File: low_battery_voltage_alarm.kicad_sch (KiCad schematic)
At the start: 20 parts, among them J1 V-DISPLAY, Q1 2N4401, Q2 2N4401, SW1 SW_DIP_x01, U1 NE555P

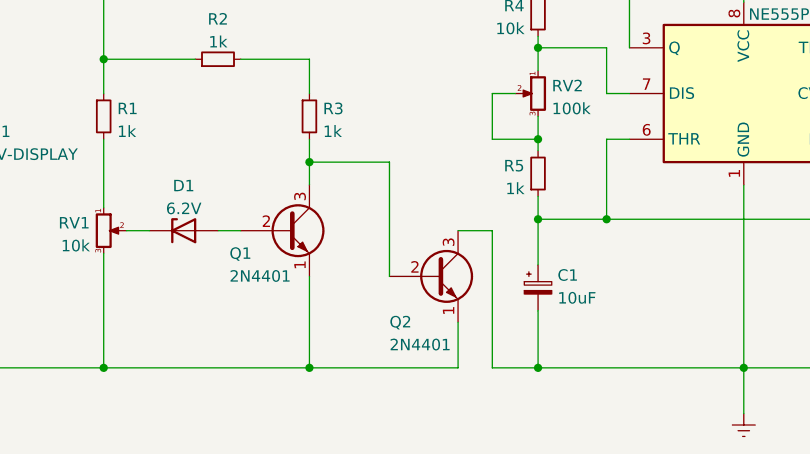
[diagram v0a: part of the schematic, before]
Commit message: change 2N4401 => MMBT4401
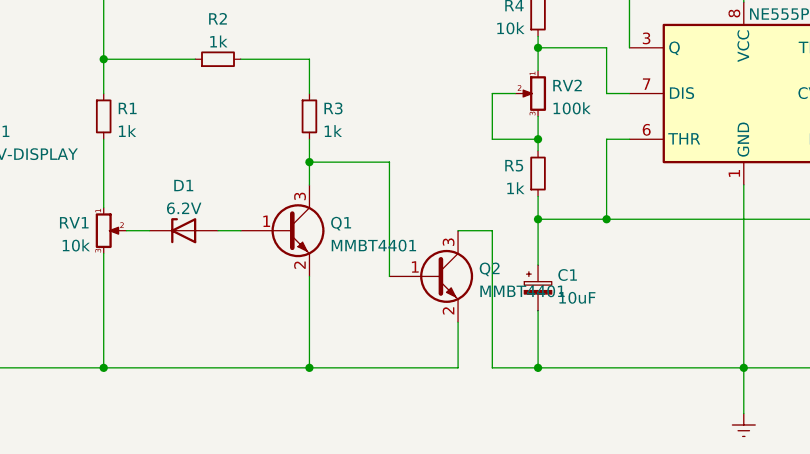
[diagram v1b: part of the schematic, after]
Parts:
- removed Q1, Q2: 2N4401, Package_TO_SOT_SMD:SOT-23, symbol Transistor_BJT:2N2219
- added Q1, Q2: MMBT4401, Package_TO_SOT_SMD:SOT-23, symbol Transistor_BJT:MMBT3904
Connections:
- net GNDREF: now also Q2.3 (C)
- net at BT1.2 (-), J1.2 (Pin_2), RV1.3: now also Q1.2 (E), Q2.2 (E)
- net at R3.2: now also Q1.3 (C), Q2.1 (B)
- net at D1.2 (A): now also Q1.1 (B)

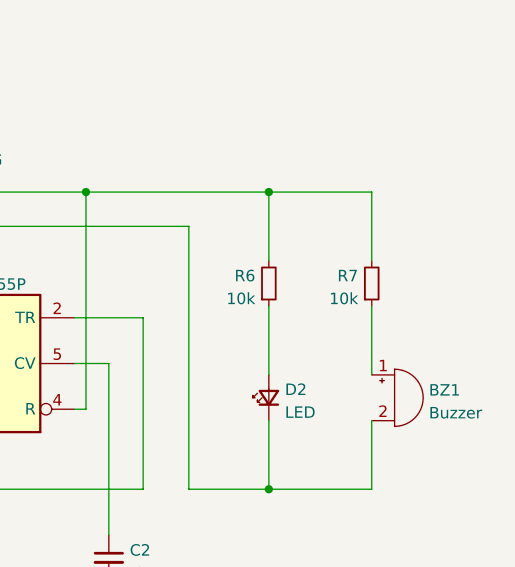
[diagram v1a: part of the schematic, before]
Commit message: change footprint error and add jumper to buzzer(mini power)
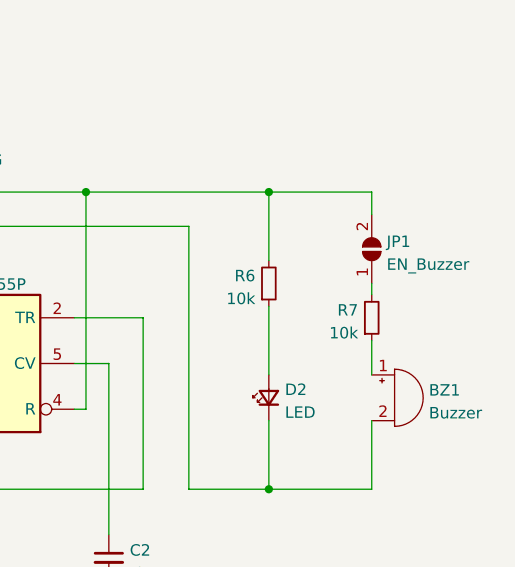
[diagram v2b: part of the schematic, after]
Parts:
- added JP1: EN_Buzzer, Jumper:SolderJumper-2_P1.3mm_Open_RoundedPad1.0x1.5mm, symbol Jumper:SolderJumper_2_Open
- D1: footprint Diode_SMD:D_MicroMELF_Handsoldering -> Diode_THT:D_DO-35_SOD27_P7.62mm_Horizontal
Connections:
- net at R1.1, R2.1, R4.2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: now also JP1.2 (B); no longer R7.2
- new net: JP1.1 (A), R7.2
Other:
- moved on the sheet: R7
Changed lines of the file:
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@@
     (stroke (width 0) (type default) (color 0 0 0 0))
   )
-  (wire (pts (xy 200.66 91.44) (xy 200.66 99.06))
+  (wire (pts (xy 200.66 88.9) (xy 200.66 90.17))
+    (stroke (width 0) (type default) (color 0 0 0 0))
+  )
+  (wire (pts (xy 200.66 95.25) (xy 200.66 99.06))
     (stroke (width 0) (type default) (color 0 0 0 0))
   )
@@
     (stroke (width 0) (type default) (color 0 0 0 0))
   )
-  (wire (pts (xy 200.66 78.74) (xy 200.66 86.36))
+  (wire (pts (xy 200.66 78.74) (xy 200.66 81.28))
     (stroke (width 0) (type default) (color 0 0 0 0))
   )
@@
     )
     (property "Datasheet" "~" (id 3) (at 202.565 99.06 90)
+      (effects (font (size 1.27 1.27)) hide)
+    )
+    (pin "1")
+    (pin "2")
+  )
+  (symbol (lib_id "Jumper:SolderJumper_2_Open") (at 200.66 85.09 90) (unit 1)
+    (in_bom yes) (on_board yes) (fields_autoplaced)
+    (property "Reference" "JP1" (id 0) (at 202.311 84.2553 90)
+      (effects (font (size 1.27 1.27)) (justify right))
+    )
+    (property "Value" "EN_Buzzer" (id 1) (at 202.311 86.7922 90)
+      (effects (font (size 1.27 1.27)) (justify right))
+    )
+    (property "Footprint" "Jumper:SolderJumper-2_P1.3mm_Open_RoundedPad1.0x1.5mm" (id 2) (at 200.66 85.09 0)
+      (effects (font (size 1.27 1.27)) hide)
+    )
+    (property "Datasheet" "~" (id 3) (at 200.66 85.09 0)
       (effects (font (size 1.27 1.27)) hide)
     )
@@
     (property "Reference" "D1" (id 0) (at 92.71 108.0602 0))
     (property "Value" "6.2V" (id 1) (at 92.71 110.5971 0))
-    (property "Footprint" "Diode_SMD:D_MicroMELF_Handsoldering" (id 2) (at 92.71 113.03 0)
+    (property "Footprint" "Diode_THT:D_DO-35_SOD27_P7.62mm_Horizontal" (id 2) (at 92.71 113.03 0)
       (effects (font (size 1.27 1.27)) hide)
     )
@@
     (pin "2")
   )
-  (symbol (lib_id "Device:R_Small") (at 200.66 88.9 0) (mirror x) (unit 1)
-    (in_bom yes) (on_board yes) (fields_autoplaced)
-    (property "Reference" "R7" (id 0) (at 199.1615 88.0653 0)
-      (effects (font (size 1.27 1.27)) (justify right))
-    )
-    (property "Value" "10k" (id 1) (at 199.1615 90.6022 0)
-      (effects (font (size 1.27 1.27)) (justify right))
-    )
-    (property "Footprint" "Resistor_SMD:R_0805_2012Metric_Pad1.20x1.40mm_HandSolder" (id 2) (at 200.66 88.9 0)
-      (effects (font (size 1.27 1.27)) hide)
-    )
-    (property "Datasheet" "~" (id 3) (at 200.66 88.9 0)
+  (symbol (lib_id "Device:R_Small") (at 200.66 92.71 0) (mirror x) (unit 1)
+    (in_bom yes) (on_board yes) (fields_autoplaced)
+    (property "Reference" "R7" (id 0) (at 199.1615 91.8753 0)
+      (effects (font (size 1.27 1.27)) (justify right))
+    )
+    (property "Value" "10k" (id 1) (at 199.1615 94.4122 0)
+      (effects (font (size 1.27 1.27)) (justify right))
+    )
+    (property "Footprint" "Resistor_SMD:R_0805_2012Metric_Pad1.20x1.40mm_HandSolder" (id 2) (at 200.66 92.71 0)
+      (effects (font (size 1.27 1.27)) hide)
+    )
+    (property "Datasheet" "~" (id 3) (at 200.66 92.71 0)
       (effects (font (size 1.27 1.27)) hide)
     )
@@
     )
     (path "/b20c0d4e-487e-4f58-92dd-72be7069083b"
-      (reference "D1") (unit 1) (value "6.2V") (footprint "Diode_SMD:D_MicroMELF_Handsoldering")
+      (reference "D1") (unit 1) (value "6.2V") (footprint "Diode_THT:D_DO-35_SOD27_P7.62mm_Horizontal")
     )
     (path "/f72c2460-da37-40cc-bc67-bdf402bec378"
@@
       (reference "J1") (unit 1) (value "V-DISPLAY") (footprint "Connector_JST:JST_XH_S2B-XH-A-1_1x02_P2.50mm_Horizontal")
     )
+    (path "/752fd9d4-9ebc-457c-9a29-e66a22cf32bb"
+      (reference "JP1") (unit 1) (value "EN_Buzzer") (footprint "Jumper:SolderJumper-2_P1.3mm_Open_RoundedPad1.0x1.5mm")
+    )
     (path "/03b95f6c-6b31-486a-bbd3-22a7f8e08333"
